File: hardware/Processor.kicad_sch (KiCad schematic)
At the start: 27 parts, among them Q3 2N7002DW, Q4 DMN65D8L-7, SW1 B3U-1000P-B, SW2 B3U-1000P-B, U1 TM4C123GH6PM, X1 TXC-7C

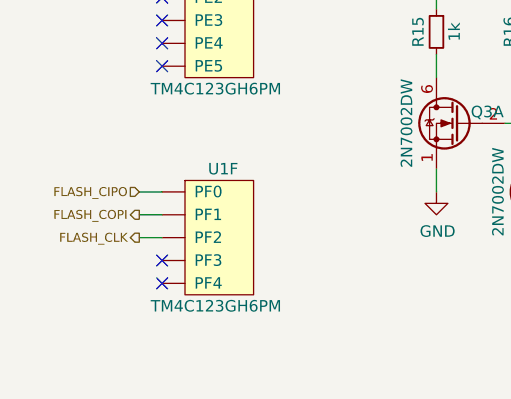
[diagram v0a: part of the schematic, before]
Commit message: Added control for the level shifter output enable to the CPU to fix problems caused by us accidentally still driving the external bus after reset is released
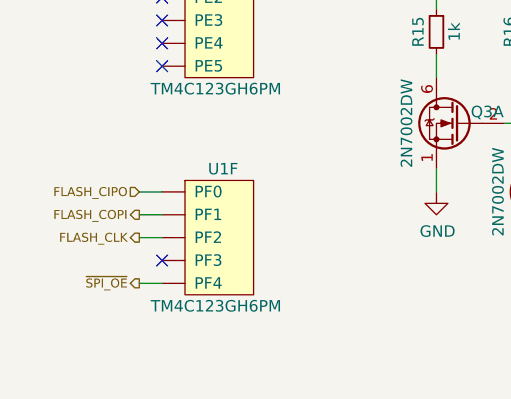
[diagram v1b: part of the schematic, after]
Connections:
- net ~{SPI_OE}: now reaches U1.5 (PF4)
- no-connect marks 25 -> 24
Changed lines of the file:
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@@
   (no_connect (at 69.85 138.43))
   (no_connect (at 128.27 105.41))
-  (no_connect (at 69.85 170.18))
   (no_connect (at 204.47 143.51))
   (no_connect (at 148.59 173.99))
@@
     (stroke (width 0) (type default) (color 0 0 0 0))
   )
+  (wire (pts (xy 67.31 170.18) (xy 69.85 170.18))
+    (stroke (width 0) (type default) (color 0 0 0 0))
+  )
   (wire (pts (xy 118.11 110.49) (xy 120.65 110.49))
     (stroke (width 0) (type default) (color 0 0 0 0))
@@
   )
   (hierarchical_label "~{SPI_PRESENT}" (shape input) (at 125.73 113.03 270)
+    (effects (font (size 0.9906 0.9906)) (justify right))
+  )
+  (hierarchical_label "~{SPI_OE}" (shape output) (at 67.31 170.18 180)
     (effects (font (size 0.9906 0.9906)) (justify right))
   )
@@
     (pin "1")
   )
-  (symbol (lib_id "Device:Q_NMOS_GSD") (at 123.19 167.64 0) (mirror y)
+  (symbol (lib_id "Device:Q_NMOS_GSD") (at 123.19 167.64 0) (mirror y) (unit 1)
     (in_bom yes) (on_board yes)
     (property "Reference" "Q4" (id 0) (at 124.46 166.37 0)
